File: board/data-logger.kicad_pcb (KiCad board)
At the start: 6 copper layers, 60 x 80 mm, 296 parts, among them P201 CONN_01X02, P202 USB_B_3, P301 CONN_02X10, P302 CONN_02X10, P303 CONN_02X10, P601 CONN_02X05, P602 CONN_02X05, Q201 IRLML6344TRPBF, Q202 Q_NPN_BEC, Q203 CSD17313Q2, Q204 CSD17313Q2, SW201 SW_Push, U201 LM5050-1, U202 CYUSB3012-BZXC, U203 R3111xxxB, U204 SP3010-04UTG, U206 NCP6332B, U207 NCP6332B, U208 MIC23050-4YML, U209 MIC23050-SYML, U210 AP2138N-1.8TRG1, U211 TPS53015, U301 5CEFA2F23, U302 LMC6062, U303 FSA5157P6X, U304 FSA5157P6X, U305 LMC6062, U306 FSA5157P6X, U401 IS43TR16256LA, U402 DSC1103CI5-100.0000, U403 NCP51200, U501 25LC_EEPROM, U502 LSF0108, U503 CDCE913, X501 CONN_DEBUG_MCNET, Y501 19.200MHz

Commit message: Rework schematic
- use better capacitors
- drop several, probably unneeded components
- make connectors PMOD compatible
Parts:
- removed C203, C223: 10µF, Capacitors_SMD:C_0603
- removed C219, C304, C306, C308, C517, C519, C521, C623, C627: 100n, Capacitors_SMD:C_0402
- removed C303, C416, C418, C421, C423, C502, C503, C504, C505, C506, C508, C509, C510, C512, C513, C514, C516, C520, C601, C602, C607, C608, C609, C610, C611, C612, C617, C619, C621, C622, C625, C626, C629: 4µ7, Capacitors_SMD:C_0402
- removed C409, C412, C413: 100nF, Resistors_SMD:R_Array_Convex_4x0402
- removed C414, C417, C419, C422, C424: 10µ, Capacitors_SMD:C_0805
- removed C518: 10p, Capacitors_SMD:C_0402
- removed C613, C614, C615, C616, C618, C620, C624, C628: 100nF, Capacitors_SMD:C_0402
- removed D201: D_TVS, Diodes_SMD:D_SMA
- removed D202: D, Diodes_SMD:D_SOT-23_ANK
- removed D205: Led_Small, LEDs:LED_0805
- removed D501, D502, D503: LED_Small, LEDs:LED_0805
- removed FB501, FB502, L204, L205: BLM18KG, Resistors_SMD:R_0603
- removed JP501, JP502: Jumper_NC_Small, Pin_Headers:Pin_Header_Straight_1x02_Pitch2.54mm
- removed L207, L208, L210: 2.2µH, AMesser_Inductors:Bourns_SRN4018TA
- removed P202: USB_B_3, AMesser_Connectors:Amphenol_GSB3211XXXWEU
- removed Q201: IRLML6344TRPBF, TO_SOT_Packages_SMD:SOT-23
- removed Q202: Q_NPN_BEC, TO_SOT_Packages_SMD:SOT-23
- removed R314, R315, R316, R317, R318, R319, R323, R324, R325, R326, R327, R328: 51R, Resistors_SMD:R_Array_Convex_4x0402
- removed R413, R501, R502, R503, R504, R505, R516, R517, R518, R520, R521, R522, R524: 10k, Resistors_SMD:R_0603
- removed R506, R507, R508: 470, Resistors_SMD:R_0603
- removed R511, R512, R513, R514, R515: 0, Resistors_SMD:R_0603
- removed R519, R530, R531, R532: 1k8, Resistors_SMD:R_0603
- removed R523: 1k, Resistors_SMD:R_0603
- removed R525: 100R, Resistors_SMD:R_0603
- removed R526, R527, R528: 4k7, Resistors_SMD:R_0603
- removed R529: 200k, Resistors_SMD:R_0603
- removed SW201: SW_Push, Pin_Headers:Pin_Header_Straight_1x02_Pitch2.54mm
- removed U201: LM5050-1, TO_SOT_Packages_SMD:SOT-23-6
- removed U203: R3111xxxB, TO_SOT_Packages_SMD:SOT-23-5
- removed U206, U207: NCP6332B, AMesser_Power_Management:ON_Semiconductor_WDFN-8_2x2mm_Pitch0.5mm
- removed U209: MIC23050-SYML, AMesser_Power_Management:Micrel_MLF-8_2x2mm_Pitch0.5mm
- removed U502: LSF0108, Housings_SSOP:TSSOP-20_4.4x6.5mm_Pitch0.65mm
- removed W201, W202: TEST_1P, Measurement_Points:Measurement_Point_Round-SMD-Pad_Small
- removed X501: CONN_DEBUG_MCNET, Pin_Headers:Pin_Header_Straight_2x05_Pitch2.54mm
- added C221, C235: 22µF/6.3V X5R, Capacitors_SMD:C_0805, F.Cu at (108.5, 172.6)
- added C230, C252, C320, C321, C322, C323, C701: 1.0µF/4.0V, AMesser_Capacitors:NFM15, F.Cu at (108.5, 172.6)
- added C238, C247, C248, C249, C250, C251, C702, C704, C705, C706, C707: 4.3µF/2.5V, AMesser_Capacitors:NFM15, F.Cu at (108.5, 172.6)
- added C703, C708, C712, C718, C719: 100n, Capacitors_SMD:C_0402, F.Cu at (108.5, 172.6)
- added C715: 1µF/16V, Capacitors_SMD:C_0402, F.Cu at (108.5, 172.6)
- added C720: 100n, Capacitors_SMD:C_1206, F.Cu at (108.5, 172.6)
- added D207, D208, D209: LED_Small, LEDs:LED_0805, F.Cu at (108.5, 172.6)
- added IC201: ATTINY2313-MU, Housings_DFN_QFN:QFN-20-1EP_4x4mm_Pitch0.5mm, F.Cu at (108.5, 172.6)
- added JP503, JP504, JP505, JP506, JP507, JP508, JP509, JP510: ~, Resistors_SMD:R_0603, F.Cu at (108.5, 172.6)
- added L602, L701, L702, L703, L704, L705: BLM18KG, Resistors_SMD:R_0603, F.Cu at (108.5, 172.6)
- added P701: USB_B_3, AMesser_Connectors:Amphenol_GSB3211XXXWEU, F.Cu at (108.5, 172.6)
- added Q205: FDG1024NZ, TO_SOT_Packages_SMD:SOT-363_SC-70-6, F.Cu at (108.5, 172.6)
- added R211: 120k n.p., Resistors_SMD:R_0603, F.Cu at (108.5, 172.6)
- added R212, R701, R702, R703: 10k, Resistors_SMD:R_Array_Convex_4x0402, F.Cu at (108.5, 172.6)
- added R213: 12.7k, Resistors_SMD:R_0603, F.Cu at (108.5, 172.6)
- added R222: 35.7k, Resistors_SMD:R_0603, F.Cu at (108.5, 172.6)
- added R224: 470, Resistors_SMD:R_Array_Convex_4x0402, F.Cu at (108.5, 172.6)
- added R225: 100k, Resistors_SMD:R_0603, F.Cu at (108.5, 172.6)
- added R227, R229, R230: 162k, Resistors_SMD:R_0603, F.Cu at (108.5, 172.6)
- added R228: 348k, Resistors_SMD:R_0603, F.Cu at (108.5, 172.6)
- added R231: 44.2k, Resistors_SMD:R_0603, F.Cu at (108.5, 172.6)
- added R232: 21k, Resistors_SMD:R_0603, F.Cu at (108.5, 172.6)
- added R233: 60.4k, Resistors_SMD:R_0603, F.Cu at (108.5, 172.6)
- added R234: 111k, Resistors_SMD:R_0603, F.Cu at (108.5, 172.6)
- added R415: 4k7, Resistors_SMD:R_0603, F.Cu at (108.5, 172.6)
- added R704: 100R, Resistors_SMD:R_0603, F.Cu at (108.5, 172.6)
- added R705: 6.04k / 1%, Resistors_SMD:R_0603, F.Cu at (108.5, 172.6)
- added R706: 200 / 1%, Resistors_SMD:R_0603, F.Cu at (108.5, 172.6)
- added R707: 1M, Resistors_SMD:R_1206, F.Cu at (108.5, 172.6)
- added TP201, TP202, TP203, TP204, TP205, TP501, TP502, TP503, TP504, TP505, TP506, TP507, TP508, TP509: TEST, Measurement_Points:Measurement_Point_Round-SMD-Pad_Small, F.Cu at (108.5, 172.6)
- added U212, U215: TLV62085, AMesser_Power_Management:Texas_Instruments-VSON-HR-7, F.Cu at (108.5, 172.6)
- added U213, U214: NCP380, AMesser_Power_Management:DFN-6-EP_2x2mm_Pitch0.65mm, F.Cu at (108.5, 172.6)
- added U307: TS881ICT, TO_SOT_Packages_SMD:SOT-353_SC-70-5, F.Cu at (108.5, 172.6)
- added U701: NCP361SNT1G, TO_SOT_Packages_SMD:TSOT-23-5, F.Cu at (108.5, 172.6)
- added U702: SP3010-04UTG, AMesser_Misc:SP3010, F.Cu at (108.5, 172.6)
- added W209: TEST_1P, Measurement_Points:Measurement_Point_Round-SMD-Pad_Small, F.Cu at (108.5, 172.6)
- added X701: CONN_DEBUG_MCNET, Pin_Headers:Pin_Header_Straight_2x05_Pitch2.54mm, F.Cu at (108.5, 172.6)
- added X702: ASDMB-19.200MHZ-LC-T, AMesser_Oscillators:Abracon_ASDMB, F.Cu at (108.5, 172.6)
- C201: value 4.3µF/2.5V -> 1µF/16V; footprint Capacitors_SMD:C_0402 -> Capacitors_SMD:C_0603
- C202: value 4.7µF -> 0.1µF/16V
- C204: value 10µF -> 1µF/35V
- C205: value 4.7µF -> 120µF/35V; footprint Capacitors_SMD:C_0402 -> Capacitors_ThroughHole:CP_Radial_D10.0mm_P5.00mm
- C206, C210: value 4.7µF -> 22µF/6.3V X5R; footprint Capacitors_SMD:C_0402 -> Capacitors_SMD:C_0805
- C207, C218, C405: value 100n -> 1.0µF/4.0V; footprint Capacitors_SMD:C_0402 -> AMesser_Capacitors:NFM15
- C208, C237, C239: value 10µF -> 1.0µF/4.0V; footprint Capacitors_SMD:C_0603 -> AMesser_Capacitors:NFM15
- C209, C222: value 10µF -> 22µF/6.3V X5R; footprint Capacitors_SMD:C_0603 -> Capacitors_SMD:C_0805
- C211, C212, C214, C215: value 100n -> 22µF/6.3V X5R; footprint Capacitors_SMD:C_0402 -> Capacitors_SMD:C_0805
- C213: value 100n -> 4.3µF/2.5V; footprint Capacitors_SMD:C_0402 -> AMesser_Capacitors:NFM15
- C216: value 100nF -> 22µF/6.3V X5R; footprint Capacitors_SMD:C_0402 -> Capacitors_SMD:C_0805
- C217: value 470µF -> 22µF/6.3V X5R; footprint Capacitors_ThroughHole:CP_Radial_D10.0mm_P5.00mm -> Capacitors_SMD:C_0805
- C220: value 100n -> 4.3µF/2.5V; footprint Capacitors_SMD:C_1206 -> AMesser_Capacitors:NFM15
- C224, C225, C233, C234: value 4.7µF -> 1.0µF/4.0V; footprint Capacitors_SMD:C_0402 -> AMesser_Capacitors:NFM15
- C226: value 1µF -> 4.3µF/2.5V; footprint Capacitors_SMD:C_0603 -> AMesser_Capacitors:NFM15
- C227: value 1µF -> 1.0µF/4.0V; footprint Capacitors_SMD:C_0603 -> AMesser_Capacitors:NFM15
- C229: value 560p -> 1.0µF/4.0V; footprint Capacitors_SMD:C_0402 -> AMesser_Capacitors:NFM15
- C231: value 27p -> 470µF/6.3V; footprint Capacitors_SMD:C_0402 -> Capacitors_ThroughHole:CP_Radial_D6.3mm_P2.50mm
- C232: value 27pF -> 22µF/6.3V X5R; footprint Capacitors_SMD:C_0402 -> Capacitors_SMD:C_0805
- C236: value 10µF -> 4.3µF/2.5V; footprint Capacitors_SMD:C_0603 -> AMesser_Capacitors:NFM15
- C241: footprint Capacitors_SMD:C_0603 -> Capacitors_SMD:C_0402
- C244: value 22µF/4V -> 4.3µF/2.5V; footprint Capacitors_SMD:C_0603 -> AMesser_Capacitors:NFM15
- C245: value 22µF/4V -> 1.0µF/4.0V; footprint Capacitors_SMD:C_0603 -> AMesser_Capacitors:NFM15
- C246: value 220µF/6.3V -> 470µF/6.3V; footprint Capacitors_ThroughHole:CP_Radial_D5.0mm_P2.00mm -> Capacitors_ThroughHole:CP_Radial_D6.3mm_P2.50mm
- C301, C302, C310, C311, C312, C313, C401, C406, C501, C603, C604, C605, C606: value 4µ7 -> 1.0µF/4.0V; footprint Capacitors_SMD:C_0402 -> AMesser_Capacitors:NFM15
- C402, C403, C404: value 4µ7 -> 4.3µF/2.5V; footprint Capacitors_SMD:C_0402 -> AMesser_Capacitors:NFM15
- C407, C408: value 4µ7 -> 22µF/6.3V X5R; footprint Capacitors_SMD:C_0402 -> Capacitors_SMD:C_0805
- C511: value 4µ7 -> 10p
- L1: value 4.7µH/2.8A -> 6.8µH/4.5A
- L201: value BLM18KG -> 470nH/1.5A; footprint Resistors_SMD:R_0603 -> AMesser_Inductors:Bourns_SRN6045TA
- L202: value BLM18KG -> 470nH/2.5A; footprint Resistors_SMD:R_0603 -> AMesser_Inductors:Bourns_SRN6045TA
- L203: value BLM18KG -> 470nH/1.3A; footprint Resistors_SMD:R_0603 -> AMesser_Inductors:Bourns_SRN6045TA
- L209: value 2.2µH -> 2.2µH/0.5A; footprint AMesser_Inductors:Bourns_SRN4018TA -> Inductors_NEOSID:Neosid_Inductor_SM-NE29_SMD1008
- P301, P302, P303: value CONN_02X10 -> CONN_02X11; footprint Pin_Headers:Pin_Header_Angled_2x10_Pitch2.54mm -> Socket_Strips:Socket_Strip_Angled_2x11_Pitch2.54mm
- P601, P602: value CONN_02X05 -> CONN_02X06; footprint Pin_Headers:Pin_Header_Straight_2x05_Pitch2.54mm -> Socket_Strips:Socket_Strip_Angled_2x06_Pitch2.54mm
- R201: value 0.01 -> 0.1R; footprint Resistors_SMD:R_1206 -> Resistors_SMD:R_0805
- R202: value 4.7k -> 11k
- R203: value 4.7k -> 111k
- R204: value 100R -> 348k
- R205: value 1.5k -> 111k
- R206: value 6.04k / 1% -> 11k
- R207: value 200 / 1% -> 11k
- R208: value 10k -> 11k
- R209: value 470 -> 11k
- R210: value 1M -> 11k; footprint Resistors_SMD:R_1206 -> Resistors_SMD:R_0603
- R214, R216: value 220k 1% -> 111k
- R215: value 178k 1% -> 162k
- R217: value 69.8k 1% -> 4k7
- R218: value 4.64k -> 35.7k
- R509: value 10k -> 1k; footprint Resistors_SMD:R_0603 -> Resistors_SMD:R_Array_Convex_4x0402
- R510: footprint Resistors_SMD:R_0603 -> Resistors_SMD:R_Array_Convex_4x0402
- U204: value SP3010-04UTG -> NCP373MU13TXG; footprint AMesser_Misc:SP3010 -> AMesser_Power_Management:LLGA-12-EP_3x3mm_Pitch0.5mm
- U210: value AP2138N-1.8TRG1 -> TLV62085; footprint TO_SOT_Packages_SMD:SOT-23 -> AMesser_Power_Management:Texas_Instruments-VSON-HR-7
- U302, U305: value LMC6062 -> TS881ICT; footprint Housings_SOIC:SOIC-8_3.9x4.9mm_Pitch1.27mm -> TO_SOT_Packages_SMD:SOT-353_SC-70-5
- U503: value CDCE913 -> SI5351A-B-GT; footprint Housings_SSOP:TSSOP-14_4.4x5mm_Pitch0.65mm -> Housings_SSOP:MSOP-10_3x3mm_Pitch0.5mm
- Y501: value 19.200MHz -> 25.000MHz
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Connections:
- net /Cyclone V FX3 FIFO/FX3_SPI_MISO renamed FX3_SPI_MISO
- net /Cyclone V FX3 FIFO/FX3_SPI_MOSI renamed FX3_SPI_MOSI
- net /Cyclone V FX3 FIFO/~FLASH_CS~ renamed /FX3 Peripherals/~FX3_SPI_FLASHCS~
- C201 pad 1: VCC_1V20 -> VCC_USB
- C202 pad 1: VCC_1V20 -> GND
- C202 pad 2: GND -> VCC_3V30
- C204 pad 1: Net-(C204-Pad1) -> /FX3 USB & Power Supply/VCC_IN
- C205 pad 1: VCC_1V20 -> /FX3 USB & Power Supply/VCC_IN
- C206 pad 1: Net-(C206-Pad1) -> GND
- C206 pad 2: GND -> VCC_3V30
- C208 pad 1: Net-(C203-Pad1) -> VCC_2V50
- C209 pad 1: Net-(C204-Pad1) -> GND
- C209 pad 2: GND -> VCC_3V30
- C210 pad 1: VCC_1V20 -> GND
- C210 pad 2: GND -> VCC_3V30
- C211 pad 1: Net-(C211-Pad1) -> GND
- C211 pad 2: GND -> VCC_2V50
- C212 pad 1: Net-(C206-Pad1) -> GND
- C212 pad 2: GND -> VCC_3V30
- C213 pad 1: /FX3 USB & Power Supply/VCC_USB -> VCC_1V20
- C214 pad 1: Net-(C203-Pad1) -> GND
- C214 pad 2: GND -> VCC_1V10_FPGA
- C215 pad 1: Net-(C204-Pad1) -> GND
- C215 pad 2: GND -> VCC_1V35_FPGA
- C216 pad 1: Net-(C216-Pad1) -> GND
- C216 pad 2: GND -> VCC_3V30_FPGA
- C217 pad 1: /FX3 USB & Power Supply/VCC_IN -> GND
- C217 pad 2: GND -> VCC_2V50_FPGA
- C218 pad 1: Net-(C218-Pad1) -> VCC_3V30
- C218 pad 2: /FX3 USB & Power Supply/USB_SS_TX_N -> GND
- C220 pad 1: Net-(C220-Pad1) -> VCC_1V20
- C222 pad 1: /FX3 USB & Power Supply/VCC_IN -> GND
- C222 pad 2: GND -> VCC_2V50_FPGA
- C224 pad 1: /FX3 USB & Power Supply/VCC_IN -> VCC_3V30
- C225 pad 1: /FX3 USB & Power Supply/VCC_IN -> VCC_2V50
- C226 pad 1: VCC_2V50 -> VCC_1V20
- C227 pad 1: VCC_1V80 -> VCC_3V30_FPGA
- C229 pad 1: VCC_3V30 -> VCC_2V50_FPGA
- C229 pad 2: Net-(C229-Pad2) -> GND
- C231 pad 1: VCC_1V35 -> VCC_1V10_FPGA
- C231 pad 2: Net-(C231-Pad2) -> GND
- C232 pad 1: VCC_2V50 -> GND
- C232 pad 2: Net-(C232-Pad2) -> VCC_1V35_FPGA
- C233 pad 1: VCC_1V20 -> VCC_3V30_FPGA
- C234 pad 1: VCC_3V30 -> VCC_2V50_FPGA
- C236 pad 1: VCC_1V35 -> VCC_1V35_FPGA
- C237 pad 1: VCC_2V50 -> VCC_2V50_FPGA
- C239 pad 1: VCC_1V35 -> VCC_2V50_FPGA
- C244 pad 1: GND -> VCC_1V35_FPGA
- C244 pad 2: VCC_1V10 -> GND
- C245 pad 1: GND -> VCC_2V50_FPGA
- C245 pad 2: VCC_1V10 -> GND
- C246 pad 1: VCC_1V10 -> VCC_3V30
- C316 pad 1: VCC_3V30 -> VCC_3V30_FPGA
- C317 pad 1: VCC_3V30 -> VCC_3V30_FPGA
- C319 pad 1: VCC_3V30 -> /Cyclone V User IO/VCC_3V30
- C401 pad 1: VCC_1V35 -> Net-(C401-Pad1)
- C402 pad 1: VCC_1V35 -> /Cyclone V DDR3 RAM/VTT_DDR3
- C403 pad 1: VCC_1V35 -> /Cyclone V DDR3 RAM/VTT_DDR3
- C404 pad 1: VCC_1V35 -> /Cyclone V DDR3 RAM/VTT_DDR3
- C405 pad 1: Net-(C405-Pad1) -> VCC_2V50_FPGA
- C406 pad 1: VCC_1V35 -> VCC_2V50_FPGA
- C407 pad 1: VCC_1V35 -> GND
- C407 pad 2: GND -> VCC_1V35_FPGA
- C408 pad 1: VCC_1V35 -> GND
- C408 pad 2: GND -> /Cyclone V DDR3 RAM/VTT_DDR3
- C410 pad 1: /Cyclone V DDR3 RAM/VTT_DDR3 -> GND
- C507 pad 1: GND -> VCC_2V50
- C507 pad 2: VCC_2V50 -> GND
- C511 pad 1: VCC_2V50 -> Net-(C511-Pad1)
- C603 pad 1: VCC_1V10 -> Net-(C603-Pad1)
- C604 pad 1: VCC_1V10 -> Net-(C604-Pad1)
- C605 pad 1: VCC_1V10 -> Net-(C603-Pad1)
- C606 pad 1: VCC_1V10 -> Net-(C604-Pad1)
- D203 pad 2: Net-(D202-Pad2) -> Net-(D203-Pad2)
- D204 pad 1: /FX3 USB & Power Supply/VCC_IN -> GND
- D204 pad 2: GND -> Net-(D203-Pad2)
- FB401 pad 1: VCC_2V50 -> VCC_2V50_FPGA
- FB401 pad 2: Net-(C405-Pad1) -> Net-(C401-Pad1)
- L1 pad 2: VCC_1V10 -> VCC_3V30
- L201 pad 1: VCC_2V50 -> Net-(L201-Pad1)
- L201 pad 2: Net-(C211-Pad1) -> VCC_2V50
- L202 pad 1: VCC_1V20 -> Net-(L202-Pad1)
- L202 pad 2: Net-(C206-Pad1) -> VCC_1V10_FPGA
- L203 pad 1: VCC_1V20 -> Net-(L203-Pad1)
- L203 pad 2: Net-(C203-Pad1) -> VCC_1V35_FPGA
- L601 pad 1: VCC_2V50 -> VCC_2V50_FPGA
- L601 pad 2: Net-(C617-Pad1) -> Net-(C604-Pad1)
- P301 pad 1: VCC_3V30 -> VCC_2V50_FPGA
- P301 pad 10: /Cyclone V User IO/IO_A2_N -> /Cyclone V User IO/IO_A1_N
- P301 pad 11: /Cyclone V User IO/IO_A3_P -> /Cyclone V User IO/IO_A2_P
- P301 pad 12: /Cyclone V User IO/IO_A3_N -> /Cyclone V User IO/IO_A2_N
- P301 pad 13: /Cyclone V User IO/IO_A4_P -> /Cyclone V User IO/IO_A3_P
- P301 pad 14: /Cyclone V User IO/IO_A4_N -> /Cyclone V User IO/IO_A3_N
- P301 pad 15: /Cyclone V User IO/IO_A5_P -> /Cyclone V User IO/IO_A4_P
- P301 pad 16: /Cyclone V User IO/IO_A5_N -> /Cyclone V User IO/IO_A4_N
- P301 pad 17: /Cyclone V User IO/IO_A6_P -> /Cyclone V User IO/IO_A5_P
- P301 pad 18: /Cyclone V User IO/IO_A6_N -> /Cyclone V User IO/IO_A5_N
- P301 pad 19: /Cyclone V User IO/IO_A7_P -> /Cyclone V User IO/IO_A6_P
- P301 pad 2: /Cyclone V User IO/VCCIO_IO_A_IN -> VCC_3V30_FPGA
- P301 pad 20: /Cyclone V User IO/IO_A7_N -> /Cyclone V User IO/IO_A6_N
- P301 pad 3: GND -> /Cyclone V User IO/VCCIO_IO_A_IN
- P301 pad 4: VCC_2V50 -> /Cyclone V User IO/VCCIO_IO_A_IN
- P301 pad 5: /Cyclone V User IO/IO_A0_P -> GND
- P301 pad 6: /Cyclone V User IO/IO_A0_N -> GND
- P301 pad 7: /Cyclone V User IO/IO_A1_P -> /Cyclone V User IO/IO_A0_P
- P301 pad 8: /Cyclone V User IO/IO_A1_N -> /Cyclone V User IO/IO_A0_N
- P301 pad 9: /Cyclone V User IO/IO_A2_P -> /Cyclone V User IO/IO_A1_P
- P302 pad 1: VCC_3V30 -> VCC_2V50_FPGA
- P302 pad 10: /Cyclone V User IO/IO_B2_N -> /Cyclone V User IO/IO_B1_N
- P302 pad 11: /Cyclone V User IO/IO_B3_P -> /Cyclone V User IO/IO_B2_P
- P302 pad 12: /Cyclone V User IO/IO_B3_N -> /Cyclone V User IO/IO_B2_N
- P302 pad 13: /Cyclone V User IO/IO_B4_P -> /Cyclone V User IO/IO_B3_P
- P302 pad 14: /Cyclone V User IO/IO_B4_N -> /Cyclone V User IO/IO_B3_N
- P302 pad 15: /Cyclone V User IO/IO_B5_P -> /Cyclone V User IO/IO_B4_P
- P302 pad 16: /Cyclone V User IO/IO_B5_N -> /Cyclone V User IO/IO_B4_N
- P302 pad 17: /Cyclone V User IO/IO_B6_P -> /Cyclone V User IO/IO_B5_P
- P302 pad 18: /Cyclone V User IO/IO_B6_N -> /Cyclone V User IO/IO_B5_N
- P302 pad 19: /Cyclone V User IO/IO_B7_P -> /Cyclone V User IO/IO_B6_P
- P302 pad 2: /Cyclone V User IO/VCCIO_IO_B -> VCC_3V30_FPGA
- P302 pad 20: /Cyclone V User IO/IO_B7_N -> /Cyclone V User IO/IO_B6_N
- P302 pad 3: GND -> /Cyclone V User IO/VCCIO_IO_B
- P302 pad 4: VCC_2V50 -> /Cyclone V User IO/VCCIO_IO_B
- P302 pad 5: /Cyclone V User IO/IO_B0_P -> GND
- P302 pad 6: /Cyclone V User IO/IO_B0_N -> GND
- P302 pad 7: /Cyclone V User IO/IO_B1_P -> /Cyclone V User IO/IO_B0_P
- P302 pad 8: /Cyclone V User IO/IO_B1_N -> /Cyclone V User IO/IO_B0_N
- P302 pad 9: /Cyclone V User IO/IO_B2_P -> /Cyclone V User IO/IO_B1_P
- P303 pad 1: VCC_3V30 -> VCC_2V50_FPGA
- P303 pad 10: /Cyclone V User IO/IO_C2_N -> /Cyclone V User IO/IO_C1_N
- P303 pad 11: /Cyclone V User IO/IO_C3_P -> /Cyclone V User IO/IO_C2_P
- P303 pad 12: /Cyclone V User IO/IO_C3_N -> /Cyclone V User IO/IO_C2_N
- P303 pad 13: /Cyclone V User IO/IO_C4_P -> /Cyclone V User IO/IO_C3_P
- P303 pad 14: /Cyclone V User IO/IO_C4_N -> /Cyclone V User IO/IO_C3_N
- P303 pad 15: /Cyclone V User IO/IO_C5_P -> /Cyclone V User IO/IO_C4_P
- P303 pad 16: /Cyclone V User IO/IO_C5_N -> /Cyclone V User IO/IO_C4_N
- P303 pad 17: /Cyclone V User IO/IO_C6_P -> /Cyclone V User IO/IO_C5_P
- P303 pad 18: /Cyclone V User IO/IO_C6_N -> /Cyclone V User IO/IO_C5_N
- P303 pad 19: /Cyclone V User IO/IO_C7_P -> /Cyclone V User IO/IO_C6_P
- P303 pad 2: /Cyclone V User IO/VCCIO_IO_C -> VCC_3V30_FPGA
- P303 pad 20: /Cyclone V User IO/IO_C7_N -> /Cyclone V User IO/IO_C6_N
- P303 pad 3: GND -> /Cyclone V User IO/VCCIO_IO_C
- P303 pad 4: VCC_2V50 -> /Cyclone V User IO/VCCIO_IO_C
- P303 pad 5: /Cyclone V User IO/IO_C0_P -> GND
- P303 pad 6: /Cyclone V User IO/IO_C0_N -> GND
- P303 pad 7: /Cyclone V User IO/IO_C1_P -> /Cyclone V User IO/IO_C0_P
- P303 pad 8: /Cyclone V User IO/IO_C1_N -> /Cyclone V User IO/IO_C0_N
- P303 pad 9: /Cyclone V User IO/IO_C2_P -> /Cyclone V User IO/IO_C1_P
- P601 pad 1: VCC_3V30 -> VCC_3V30_FPGA
- P601 pad 10: /Cyclone V Power/EXT_IO7 -> /Cyclone V Power/EXT_IO5
- P601 pad 2: GND -> VCC_3V30_FPGA
- P601 pad 3: /Cyclone V Power/EXT_IO0 -> GND
- P601 pad 4: /Cyclone V Power/EXT_IO1 -> GND
- P601 pad 5: /Cyclone V Power/EXT_IO2 -> /Cyclone V Power/EXT_IO0
- P601 pad 6: /Cyclone V Power/EXT_IO3 -> /Cyclone V Power/EXT_IO1
- P601 pad 7: /Cyclone V Power/EXT_IO4 -> /Cyclone V Power/EXT_IO2
- P601 pad 8: /Cyclone V Power/EXT_IO5 -> /Cyclone V Power/EXT_IO3
- P601 pad 9: /Cyclone V Power/EXT_IO6 -> /Cyclone V Power/EXT_IO4
- P602 pad 1: VCC_3V30 -> Net-(P602-Pad1)
- P602 pad 10: /Cyclone V Power/EXT_IO15 -> /Cyclone V Power/EXT_IO13
- P602 pad 2: GND -> Net-(P602-Pad1)
- P602 pad 3: /Cyclone V Power/EXT_IO8 -> GND
- P602 pad 4: /Cyclone V Power/EXT_IO9 -> GND
- P602 pad 5: /Cyclone V Power/EXT_IO10 -> /Cyclone V Power/EXT_IO8
- P602 pad 6: /Cyclone V Power/EXT_IO11 -> /Cyclone V Power/EXT_IO9
- P602 pad 7: /Cyclone V Power/EXT_IO12 -> /Cyclone V Power/EXT_IO10
- P602 pad 8: /Cyclone V Power/EXT_IO13 -> /Cyclone V Power/EXT_IO11
- P602 pad 9: /Cyclone V Power/EXT_IO14 -> /Cyclone V Power/EXT_IO12
- R201 pad 1: Net-(D202-Pad2) -> Net-(D203-Pad2)
- R202 pad 1: Net-(D202-Pad1) -> /FX3 USB & Power Supply/~ATTINY_RESET~
- R202 pad 2: Net-(R202-Pad2) -> VCC_3V30
- R203 pad 1: Net-(R202-Pad2) -> Net-(IC201-Pad20)
- R204 pad 1: /FX3 USB & Power Supply/VCC_IN -> Net-(Q205-Pad3)
- R204 pad 2: Net-(C216-Pad1) -> GND
- R205 pad 1: Net-(D205-Pad1) -> GND
- R205 pad 2: GND -> Net-(IC201-Pad1)
- R206 pad 1: Net-(R206-Pad1) -> VCC_USB
- R206 pad 2: GND -> Net-(R206-Pad2)
- R207 pad 1: Net-(R207-Pad1) -> Net-(R206-Pad2)
- R208 pad 1: Net-(Q202-Pad1) -> Net-(R208-Pad1)
- R208 pad 2: ~RESET~ -> VCC_3V30
- R209 pad 1: Net-(D206-Pad2) -> Net-(IC201-Pad11)
- R209 pad 2: VCC_3V30 -> VCC_1V20
- R210 pad 1: Net-(C220-Pad1) -> Net-(R210-Pad1)
- R214 pad 1: VCC_1V35 -> GND
- R214 pad 2: Net-(C231-Pad2) -> /FX3 USB & Power Supply/FPGA_PWREN
- R215 pad 1: Net-(C231-Pad2) -> GND
- R215 pad 2: GND -> Net-(IC201-Pad11)
- R216 pad 1: VCC_2V50 -> GND
- R216 pad 2: Net-(C232-Pad2) -> ~RESET~
- R217 pad 1: Net-(C232-Pad2) -> Net-(IC201-Pad2)
- R217 pad 2: GND -> ~RESET~
- R218 pad 1: Net-(R218-Pad1) -> VCC_3V30
- R218 pad 2: VCC_1V10 -> Net-(R218-Pad2)
- R219 pad 2: Net-(R218-Pad1) -> Net-(R218-Pad2)
- R220 pad 1: GND -> Net-(Q204-Pad2)
- R220 pad 2: Net-(Q204-Pad2) -> GND
- R308 pad 1: VCC_2V50 -> VCC_2V50_FPGA
- R310 pad 1: VCC_2V50 -> VCC_2V50_FPGA
- R320 pad 1: VCC_2V50 -> VCC_2V50_FPGA
- R405 pad 1: Net-(R405-Pad1) -> (no net)
- R407 pad 1: Net-(R407-Pad1) -> (no net)
- R407 pad 4: Net-(R407-Pad4) -> (no net)
- R411 pad 1: VCC_1V35 -> VCC_1V35_FPGA
- R509 pad 1: /Cyclone V FX3 FIFO/~FPGA_CS~ -> /Cyclone V FX3 FIFO/JTAG_FPGA_TDI
- R509 pad 2: VCC_2V50 -> /Cyclone V FX3 FIFO/JTAG_FPGA_TMS
- R510 pad 1: /Cyclone V FX3 FIFO/FX3_SPI_CLK -> VCC_2V50_FPGA
- R510 pad 2: VCC_2V50 -> (no net)
- U202 pad A10: /FX3 USB & Power Supply/USB_D_N -> /FX3 Peripherals/USB_D_N
- U202 pad A11: Net-(U202-PadA11) -> (no net)
- U202 pad A2: Net-(C203-Pad1) -> Net-(C704-Pad1)
- U202 pad A3: /FX3 USB & Power Supply/USB_SS_RX_N -> /FX3 Peripherals/USB_SS_RX_N
- U202 pad A4: /FX3 USB & Power Supply/USB_SS_RX_P -> /FX3 Peripherals/USB_SS_RX_P
- U202 pad A6: Net-(C218-Pad1) -> Net-(C718-Pad1)
- U202 pad A7: Net-(C206-Pad1) -> Net-(C702-Pad1)
- U202 pad A9: /FX3 USB & Power Supply/USB_D_P -> /FX3 Peripherals/USB_D_P
- U202 pad B11: /Cyclone V FX3 FIFO/~JTAG_TRST~ -> /FX3 Peripherals/~JTAG_FX3_TRST~
- U202 pad B3: Net-(R207-Pad1) -> Net-(R706-Pad1)
- U202 pad B5: Net-(C204-Pad1) -> Net-(C705-Pad1)
- U202 pad B6: Net-(C211-Pad1) -> Net-(C701-Pad1)
- U202 pad C10: Net-(R505-Pad1) -> /FX3 Peripherals/JTAG_FX3_TDO
- U202 pad C4: /Cyclone V FX3 FIFO/~FPGA_CS~ -> ~FX3_SPI_FPGACS~
- U202 pad C6: Net-(U202-PadC6) -> (no net)
- U202 pad C7: Net-(U202-PadC7) -> (no net)
- U202 pad C8: Net-(R206-Pad1) -> Net-(R705-Pad1)
- U202 pad C9: Net-(U202-PadC9) -> (no net)
- U202 pad D1: /Cyclone V FX3 FIFO/FPGA_nCONFIG -> /Cyclone V FX3 FIFO/~FPGA_CONFIG~
- U202 pad D10: /Cyclone V FX3 FIFO/FX3_I2C_SDA -> FX3_I2C_SDA
- U202 pad D11: /Cyclone V FX3 FIFO/FX3_LED2 -> (no net)
- U202 pad D2: /Cyclone V FX3 FIFO/FPGA_nSTATUS -> /Cyclone V FX3 FIFO/~FPGA_STATUS~
- U202 pad D4: /Cyclone V FX3 FIFO/FX3_SPI_CLK -> FX3_SPI_CLK
- U202 pad D6: Net-(U202-PadD6) -> (no net)
- U202 pad D7: /Cyclone V FX3 FIFO/FX3_CLKIN -> Net-(U202-PadD7)
- U202 pad D9: /Cyclone V FX3 FIFO/FX3_I2C_SCL -> FX3_I2C_SCL
- U202 pad E11: /FX3 USB & Power Supply/VCC_USB -> Net-(C715-Pad1)
- U202 pad E3: VCC_2V50 -> VCC_2V50_FPGA
- U202 pad E7: Net-(R524-Pad1) -> /FX3 Peripherals/JTAG_FX3_TDI
- U202 pad E8: /Cyclone V FX3 FIFO/JTAG_TMS -> /FX3 Peripherals/JTAG_FX3_TMS
- U202 pad F1: VCC_2V50 -> VCC_2V50_FPGA
- U202 pad F2: /Cyclone V FX3 FIFO/FX3_LED1 -> (no net)
- U202 pad F6: /Cyclone V FX3 FIFO/JTAG_TCK -> /FX3 Peripherals/JTAG_FX3_TCK
- U202 pad G4: Net-(R501-Pad2) -> /Cyclone V FX3 FIFO/PMODE0
- U202 pad G9: /Cyclone V FX3 FIFO/FPGA_FX3_D15 -> /Cyclone V FX3 FIFO/FPGA_FX3_D4
- U202 pad H4: Net-(R502-Pad2) -> /Cyclone V FX3 FIFO/PMODE1
- U202 pad H6: Net-(U202-PadH6) -> (no net)
- U202 pad K5: Net-(U202-PadK5) -> (no net)
- U202 pad L4: Net-(R503-Pad2) -> /Cyclone V FX3 FIFO/PMODE2
- U202 pad L8: /Cyclone V FX3 FIFO/FX3_LED0 -> /Cyclone V FX3 FIFO/~FPGA_FX3_INT~
- U204 pad 1: /FX3 USB & Power Supply/USB_SS_RX_N -> /FX3 USB & Power Supply/VCC_IN
- U204 pad 10: /FX3 USB & Power Supply/USB_SS_RX_N -> Net-(IC201-Pad4)
- U204 pad 2: /FX3 USB & Power Supply/USB_SS_RX_P -> /FX3 USB & Power Supply/VCC_IN
- U204 pad 4: /FX3 USB & Power Supply/USB_SS_TX_N -> GND
- U204 pad 5: /FX3 USB & Power Supply/USB_SS_TX_P -> GND
- U204 pad 6: /FX3 USB & Power Supply/USB_SS_TX_P -> GND
- U204 pad 7: /FX3 USB & Power Supply/USB_SS_TX_N -> Net-(R213-Pad1)
- U204 pad 8: GND -> Net-(R210-Pad1)
- U204 pad 9: /FX3 USB & Power Supply/USB_SS_RX_P -> Net-(R206-Pad2)
- U208 pad 2: /FX3 USB & Power Supply/PG_1V10 -> Net-(R208-Pad1)
- U208 pad 7: /FX3 USB & Power Supply/VCC_IN -> VCC_3V30
- U210 pad 1: GND -> Net-(R208-Pad1)
- U210 pad 2: VCC_1V80 -> /FX3 USB & Power Supply/~ATTINY_RESET~
- U210 pad 3: VCC_2V50 -> Net-(R227-Pad1)
- U211 pad 1: Net-(R218-Pad1) -> Net-(R218-Pad2)
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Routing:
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- added copper zone on In1.Cu, net VCC_2V50_FPGA
- removed copper zone on In1.Cu, net VCC_2V50
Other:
- outline, holes or cut-outs redrawn
- net class 50Ohm_Impedance: clearance 0.102 -> 0.125; via_drill 0.254 -> 0.2
- net class DDR3_100Ohm: clearance 0.102 -> 0.125; trace_width 0.102 -> 0.125; via_drill 0.254 -> 0.2
- net class DDR3_50Ohm: clearance 0.102 -> 0.125; trace_width 0.102 -> 0.125; via_drill 0.254 -> 0.2
- net class Default: clearance 0.102 -> 0.125; trace_width 0.102 -> 0.125; via_drill 0.254 -> 0.2
- rule trace_clearance: 0.102 -> 0.125
- rule trace_min: 0.102 -> 0.125
- rule via_min_drill: 0.254 -> 0.2
- rule via_min_size: 0.458 -> 0.46

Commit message: PCB Layout
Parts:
- removed C411: 100n n.p., Capacitors_SMD:C_0402
- removed R407: 51R, Resistors_SMD:R_Array_Convex_4x0402
- moved C205 14.9 mm to (123.0, 176.2)
- moved C231 7.86 mm to (81.9, 95.2)
- moved C407 3.80 mm to (97.0, 86.3), turned to 270 degrees
- moved C415 1.77 mm to (93.7, 89.2), turned to 180 degrees
- moved C405 1.61 mm to (90.6, 87.9)
- moved R411 1.36 mm to (95.0, 90.4), turned to 180 degrees
- moved C406 1.00 mm to (89.6, 87.9)
- moved U403 0.95 mm to (93.7, 86.9)
- moved C408 0.50 mm to (99.2, 86.3)
- moved R412 0.45 mm to (92.4, 90.4), turned to 180 degrees
- moved C420 0.10 mm to (90.4, 85.9), turned to 270 degrees
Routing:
- net VCC_1V10_FPGA: track 35.8 -> 6.54 mm, vias 24 -> 12
- net GND: track 110.9 -> 92.8 mm, vias 98 -> 100
- net (no net): track 43.3 -> 30.9 mm, vias 28 -> 16
- net VCC_1V35_FPGA: track 42.4 -> 32.0 mm
- net /Cyclone V DDR3 RAM/VTT_DDR3: track 32.7 -> 39.6 mm, vias 5 -> 7
- net Net-(C411-Pad2): track 1.62 -> 0.00 mm
- net /Cyclone V DDR3 RAM/VREF_DDR3: track 51.3 -> 52.9 mm, vias 3 -> 4
- net Net-(C415-Pad1): track 5.58 -> 4.31 mm
- net /Cyclone V DDR3 RAM/FPGA_CLK10_P: track 21.5 -> 20.7 mm
- net /Cyclone V DDR3 RAM/FPGA_CLK10_N: track 21.4 -> 20.6 mm
- net VCC_2V50_FPGA: track 11.8 -> 12.6 mm, vias 17 -> 12
- net /FX3 USB & Power Supply/FPGA_PWREN: track 0.75 -> 0.00 mm
- net Net-(IC201-Pad11): track 0.50 -> 0.00 mm, vias 1 -> 0
- added copper zone on B.Cu, net VCC_1V35_FPGA
- added copper zone on F.Cu, net VCC_1V35_FPGA
- added copper zone on F.Cu, net VCC_2V50_FPGA
- removed copper zone on F.Cu, net /FX3 USB & Power Supply/VCC_IN
- removed copper zone on In4.Cu, net GND
- removed copper zone on F.Cu, net Net-(L207-Pad1)
- removed copper zone on B.Cu, net VCC_1V35
- removed copper zone on F.Cu, net VCC_1V35

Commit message: PCB Lacout work
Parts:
- moved C250 88.4 mm to (103.8, 84.3)
- moved C248 87.7 mm to (118.1, 85.4)
- moved L203 79.4 mm to (93.9, 94.5), turned to 90 degrees
- moved C232 76.4 mm to (115.4, 96.5), turned to 180 degrees
- moved C212 75.7 mm to (92.1, 98.7), turned to 180 degrees
- moved C215 74.1 mm to (95.8, 99.6), turned to 90 degrees
- moved U215 73.5 mm to (92.1, 100.9), turned to 90 degrees
- moved C244 72.4 mm to (119.6, 101.0)
- moved R230 71.4 mm to (94.1, 102.6), turned to 90 degrees
- moved R234 71.3 mm to (92.0, 103.2)
- moved C229 59.5 mm to (98.5, 113.9), turned to 90 degrees
- moved C231 42.2 mm to (85.7, 137.2)
- moved R214 37.9 mm to (81.5, 132.6)
- moved R215 35.5 mm to (82.8, 128.9)
- moved C239 16.8 mm to (108.9, 100.5)
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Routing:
- net GND: track 92.8 -> 120.0 mm, vias 100 -> 107
- net VCC_1V35_FPGA: track 32.0 -> 51.0 mm, vias 37 -> 42
- net Net-(C415-Pad1): track 4.31 -> 13.8 mm, vias 0 -> 2
- net Net-(L203-Pad1): track 0.00 -> 6.18 mm
- net Net-(R230-Pad1): track 0.00 -> 3.68 mm
- net /Cyclone V DDR3 RAM/VTT_DDR3: track 39.6 -> 36.8 mm, vias 7 -> 2
- net VCC_3V30: track 0.00 -> 1.92 mm
- net (no net): track 30.9 -> 29.0 mm, vias 16 -> 15
- net Net-(C401-Pad1): track 5.90 -> 4.43 mm, vias 2 -> 0
- net /Cyclone V DDR3 RAM/FPGA_DDR3_A10: track 26.6 -> 25.7 mm
- added copper zone on F.Cu, net Net-(L203-Pad1)

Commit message: Further layout work
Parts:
- added REF**: MountingHole_3.2mm_M3, Mounting_Holes:MountingHole_3.2mm_M3, F.Cu at (82.5, 158.5)
- added REF**: MountingHole_3.2mm_M3, Mounting_Holes:MountingHole_3.2mm_M3, F.Cu at (125.5, 158.5)
- added REF**: MountingHole_3.2mm_M3, Mounting_Holes:MountingHole_3.2mm_M3, F.Cu at (125.5, 78.5)
- added REF**: MountingHole_3.2mm_M3, Mounting_Holes:MountingHole_3.2mm_M3, F.Cu at (82.5, 78.5)
- moved U503 94.4 mm to (72.2, 85.4)
- moved C246 87.2 mm to (83.6, 89.0), turned to 90 degrees
- moved P601 83.2 mm to (83.6, 93.2)
- moved R214 72.1 mm to (122.2, 192.1)
- moved R215 70.1 mm to (117.0, 190.1)
- moved L202 64.3 mm to (91.4, 110.6), turned to 90 degrees
- moved C251 62.1 mm to (98.7, 111.3), turned to 90 degrees
- moved P602 61.8 mm to (83.6, 116.0)
- moved C210 60.9 mm to (89.2, 114.8), turned to 180 degrees
- moved C249 60.3 mm to (98.7, 113.1), turned to 90 degrees
- moved C214 59.0 mm to (92.9, 115.7), turned to 90 degrees
- moved U212 58.8 mm to (89.2, 117.0), turned to 90 degrees
- moved C235 58.5 mm to (94.7, 115.7), turned to 90 degrees
- moved C238 58.5 mm to (98.7, 114.9), turned to 90 degrees
- moved C247 56.7 mm to (98.7, 116.7), turned to 90 degrees
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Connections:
- C718 pad 2: /FX3 Peripherals/USB_SS_TX_N -> Net-(C718-Pad2)
- P602 pad 1: Net-(P602-Pad1) -> VCC_3V30_FPGA
- P602 pad 2: Net-(P602-Pad1) -> VCC_3V30_FPGA
- P701 pad 8: /FX3 Peripherals/USB_SS_RX_N -> /FX3 Peripherals/USB_SS_RX_P
- P701 pad 9: /FX3 Peripherals/USB_SS_RX_P -> /FX3 Peripherals/USB_SS_RX_N
- U301 pad U20: (no net) -> FX3_I2C_SDA
- U301 pad U21: (no net) -> FX3_I2C_SCL
- U702 pad 4: /FX3 Peripherals/USB_SS_TX_N -> /FX3 Peripherals/USB_SS_TX_P
- U702 pad 5: /FX3 Peripherals/USB_SS_TX_P -> Net-(C718-Pad2)
- U702 pad 6: /FX3 Peripherals/USB_SS_TX_P -> /FX3 Peripherals/USB_SS_TX_N
- U702 pad 7: /FX3 Peripherals/USB_SS_TX_N -> /FX3 Peripherals/USB_SS_TX_P
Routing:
- net VCC_1V10_FPGA: track 6.54 -> 43.3 mm, vias 12 -> 46
- net /Cyclone V Power/EXT_IO12: track 21.9 -> 0.46 mm, vias 1 -> 0
- net /Cyclone V Power/EXT_IO7: track 20.5 -> 0.00 mm, vias 1 -> 0
- net /Cyclone V Power/EXT_IO8: track 20.6 -> 0.47 mm
- net /Cyclone V Power/EXT_IO10: track 20.8 -> 40.0 mm, vias 1 -> 0
- net GND: track 120.0 -> 138.6 mm, vias 107 -> 146
- net /Cyclone V Power/EXT_IO13: track 19.8 -> 1.24 mm
- net /Cyclone V Power/EXT_IO6: track 22.0 -> 5.29 mm, vias 1 -> 0
- net /Cyclone V Power/EXT_IO1: track 12.5 -> 26.4 mm, vias 1 -> 0
- net /Cyclone V Power/EXT_IO0: track 11.6 -> 20.5 mm, vias 1 -> 0
- net /Cyclone V Power/EXT_IO4: track 13.1 -> 19.8 mm, vias 1 -> 0
- net /Cyclone V Power/EXT_IO11: track 18.6 -> 24.9 mm, vias 1 -> 0
- net Net-(L202-Pad1): track 0.00 -> 6.18 mm
- net (no net): track 29.0 -> 35.1 mm, vias 15 -> 13
- net /Cyclone V Power/EXT_IO15: track 19.0 -> 24.5 mm, vias 1 -> 0
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- added copper zone on F.Cu, net Net-(L202-Pad1)
- added copper zone on F.Cu, net VCC_1V10_FPGA
- added copper zone on In2.Cu, net VCC_1V10_FPGA
- removed copper zone on F.Cu, net VCC_1V10
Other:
- board size 60 x 80 mm -> 58 x 88 mm

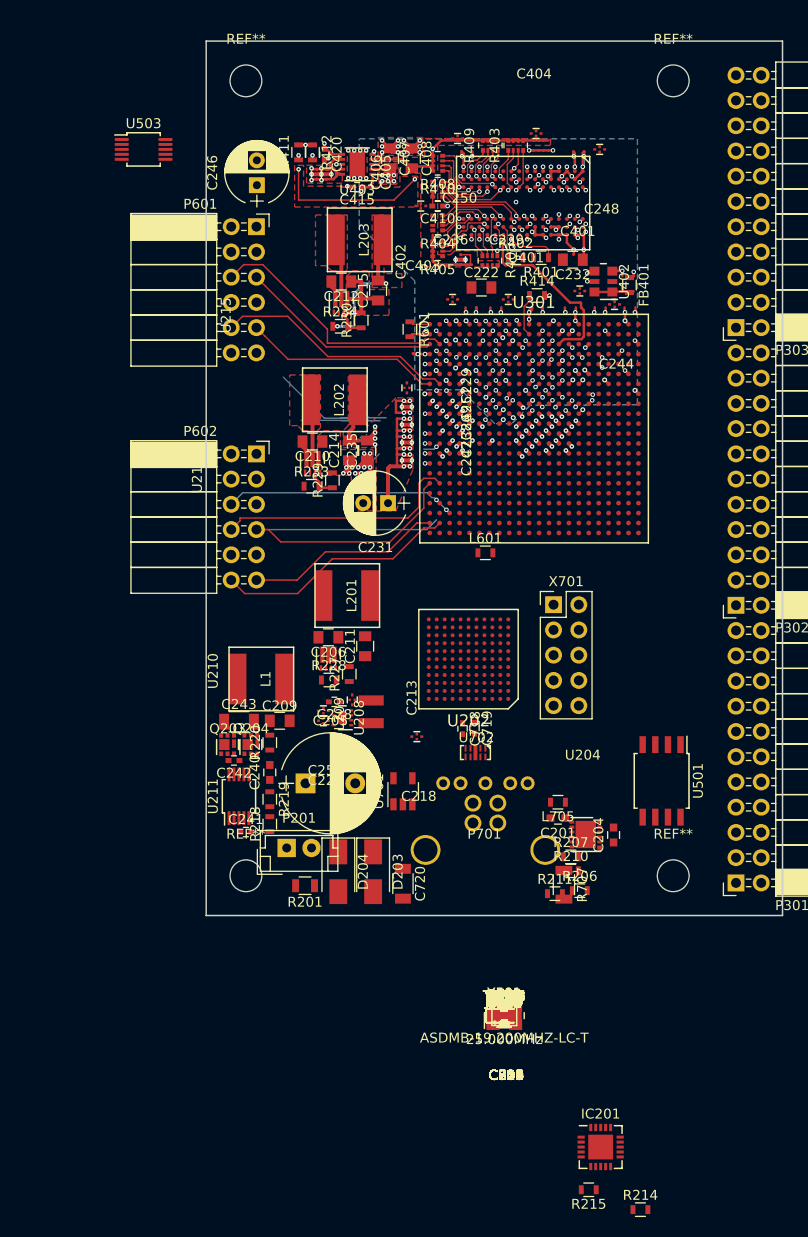
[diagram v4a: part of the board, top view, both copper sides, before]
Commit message: Initial routing work for FX3 signals
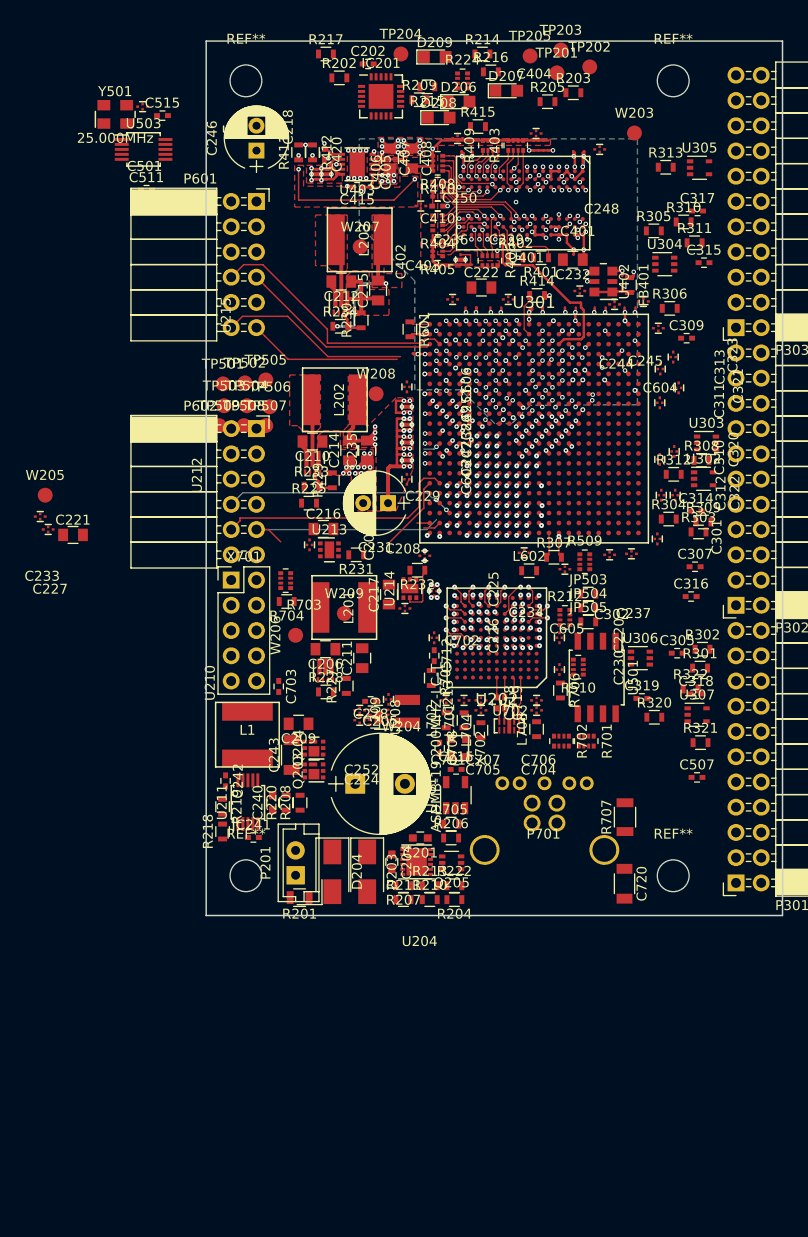
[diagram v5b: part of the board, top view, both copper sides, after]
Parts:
- removed JP506, JP507, JP508, JP509, JP510: ~, Resistors_SMD:R_0603
- removed L601: BLM18KG, Resistors_SMD:R_0603
- moved R214 117.4 mm to (106.3, 75.8)
- moved R215 112.2 mm to (100.8, 79.1)
- moved IC201 108.0 mm to (96.1, 80.1)
- moved Y501 98.8 mm to (69.3, 81.9)
- moved C501 98.5 mm to (72.1, 81.1)
- moved R217 98.4 mm to (90.5, 75.8)
- moved TP203 97.3 mm to (114.2, 75.4)
- moved TP204 97.3 mm to (98.1, 75.8)
- moved C515 96.9 mm to (74.1, 82.0)
- moved C202 96.7 mm to (94.8, 76.8)
- moved D209 96.7 mm to (101.5, 76.1)
- moved TP205 96.6 mm to (111.1, 76.0)
- moved TP202 95.9 mm to (117.1, 77.1)
- moved R202 95.8 mm to (91.9, 78.2)
- moved TP201 95.0 mm to (113.8, 77.7)
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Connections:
- C604 pad 1: Net-(C604-Pad1) -> Net-(C603-Pad1)
- C606 pad 1: Net-(C604-Pad1) -> Net-(C603-Pad1)
- Q205 pad 5: (no net) -> Net-(IC201-Pad1)
- U202 pad E3: VCC_2V50_FPGA -> VCC_2V50
- U202 pad E6: (no net) -> VCC_2V50
- U202 pad F1: VCC_2V50_FPGA -> VCC_2V50
- U301 pad D11: Net-(C604-Pad1) -> Net-(C603-Pad1)
- U301 pad D18: Net-(C604-Pad1) -> Net-(C603-Pad1)
- U301 pad E6: Net-(C604-Pad1) -> Net-(C603-Pad1)
- U301 pad W13: Net-(C604-Pad1) -> Net-(C603-Pad1)
- U301 pad W18: Net-(C604-Pad1) -> Net-(C603-Pad1)
- U301 pad W7: Net-(C604-Pad1) -> Net-(C603-Pad1)
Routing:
- net /Cyclone V Power/EXT_IO10: track 40.0 -> 7.56 mm
- net /Cyclone V Power/EXT_IO5: track 24.3 -> 0.00 mm
- net /Cyclone V Power/EXT_IO15: track 24.5 -> 1.81 mm
- net /Cyclone V FX3 FIFO/FPGA_FX3_D30: track 0.00 -> 22.2 mm, vias 0 -> 2
- net /Cyclone V Power/EXT_IO12: track 0.46 -> 21.9 mm
- net /Cyclone V Power/EXT_IO9: track 23.3 -> 1.83 mm, vias 2 -> 1
- net /Cyclone V FX3 FIFO/FPGA_FX3_D5: track 0.00 -> 21.2 mm, vias 0 -> 2
- net /Cyclone V FX3 FIFO/FPGA_FX3_D29: track 0.00 -> 19.9 mm, vias 0 -> 2
- net /Cyclone V Power/EXT_IO4: track 19.8 -> 0.00 mm
- net /Cyclone V FX3 FIFO/FPGA_FX3_FLAGB: track 0.00 -> 19.3 mm, vias 0 -> 2
- net /Cyclone V Power/EXT_IO7: track 0.00 -> 19.2 mm
- net /Cyclone V FX3 FIFO/FPGA_FX3_D28: track 0.00 -> 19.1 mm, vias 0 -> 2
- net /Cyclone V FX3 FIFO/FPGA_FX3_D31: track 0.00 -> 19.0 mm, vias 0 -> 2
- net /Cyclone V FX3 FIFO/FPGA_FX3_PKTEND: track 0.00 -> 18.5 mm, vias 0 -> 2
- net /Cyclone V Power/EXT_IO14: track 19.8 -> 1.30 mm
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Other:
- net class 50Ohm_Impedance: via_dia 0.46 -> 0.5; via_drill 0.2 -> 0.15
- net class DDR3_100Ohm: via_dia 0.46 -> 0.5; via_drill 0.2 -> 0.15
- net class DDR3_50Ohm: via_dia 0.46 -> 0.5; via_drill 0.2 -> 0.15
- net class Default: clearance 0.125 -> 0.1; trace_width 0.125 -> 0.1; via_dia 0.46 -> 0.5; via_drill 0.2 -> 0.15
- rule trace_clearance: 0.125 -> 0.1
- rule trace_min: 0.125 -> 0.1
- rule via_min_drill: 0.2 -> 0.15
- rule via_min_size: 0.46 -> 0.5

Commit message: Some pcb layout work
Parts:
- moved R305 17.2 mm to (126.8, 110.5), turned to 180 degrees
- moved R322 14.4 mm to (123.0, 153.5), turned to 90 degrees
- moved R301 14.0 mm to (117.2, 128.8)
- moved R302 13.9 mm to (117.2, 127.4), turned to 180 degrees
- moved C305 13.0 mm to (117.4, 126.3)
- moved C507 12.0 mm to (118.6, 141.0), turned to 270 degrees
- moved U304 11.7 mm to (127.1, 108.4)
- moved R208 11.6 mm to (88.5, 139.6), turned to 270 degrees
- moved C318 11.2 mm to (126.2, 151.2), turned to 90 degrees
- moved R320 11.0 mm to (124.5, 153.5), turned to 90 degrees
- moved R306 10.6 mm to (126.8, 111.9), turned to 180 degrees
- moved U307 9.34 mm to (124.2, 150.8)
- moved C307 8.81 mm to (124.3, 119.2), turned to 270 degrees
- moved R321 8.74 mm to (125.8, 153.5), turned to 90 degrees
- moved C309 8.65 mm to (126.0, 113.0)
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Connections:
- P301 pad 1: VCC_2V50_FPGA -> VCC_3V30_FPGA
- P301 pad 2: VCC_3V30_FPGA -> VCC_2V50_FPGA
- P302 pad 1: VCC_2V50_FPGA -> VCC_3V30_FPGA
- P302 pad 2: VCC_3V30_FPGA -> VCC_2V50_FPGA
- P303 pad 1: VCC_2V50_FPGA -> VCC_3V30_FPGA
- P303 pad 2: VCC_3V30_FPGA -> VCC_2V50_FPGA
- U202 pad G8: (no net) -> /Cyclone V FX3 FIFO/FPGA_FX3_D15
- U301 pad P8: (no net) -> /Cyclone V FX3 FIFO/FPGA_FX3_D15
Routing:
- net GND: track 157.1 -> 234.9 mm, vias 178 -> 231
- net Net-(C603-Pad1): track 1.20 -> 65.1 mm, vias 3 -> 1
- net /FX3 USB & Power Supply/VCC_IN: track 0.00 -> 41.4 mm
- net /Cyclone V User IO/IO_C7_N: track 0.00 -> 39.0 mm, vias 0 -> 1
- net /Cyclone V User IO/IO_C7_P: track 0.00 -> 36.7 mm, vias 0 -> 1
- net /Cyclone V User IO/IO_C6_N: track 0.00 -> 36.5 mm, vias 0 -> 1
- net /Cyclone V User IO/IO_C5_N: track 0.00 -> 34.3 mm, vias 0 -> 1
- net /Cyclone V User IO/IO_C6_P: track 0.00 -> 34.2 mm, vias 0 -> 1
- net /Cyclone V User IO/IO_C4_N: track 0.00 -> 32.3 mm, vias 0 -> 1
- net /Cyclone V User IO/IO_C3_N: track 0.00 -> 31.7 mm, vias 0 -> 1
- net /Cyclone V User IO/VCCIO_IO_A: track 0.00 -> 31.5 mm
- net /Cyclone V User IO/IO_A0_N: track 0.00 -> 31.3 mm
- net /Cyclone V User IO/IO_C5_P: track 0.00 -> 30.9 mm, vias 0 -> 1
- net /Cyclone V User IO/IO_A0_P: track 0.00 -> 29.5 mm
- net /Cyclone V User IO/IO_C2_N: track 0.00 -> 29.4 mm, vias 0 -> 1
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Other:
- net class DDR3_100Ohm: trace_width 0.125 -> 0.1
- net class DDR3_50Ohm: trace_width 0.125 -> 0.1
